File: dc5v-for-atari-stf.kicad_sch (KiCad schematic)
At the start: 13 parts, among them J1 Conn_01x02, J2 Conn_01x06, J3 Adjustable MT3608 module, J4 Fixed 12V module, J5 Conn_01x02, SW1 Momentary or Latched

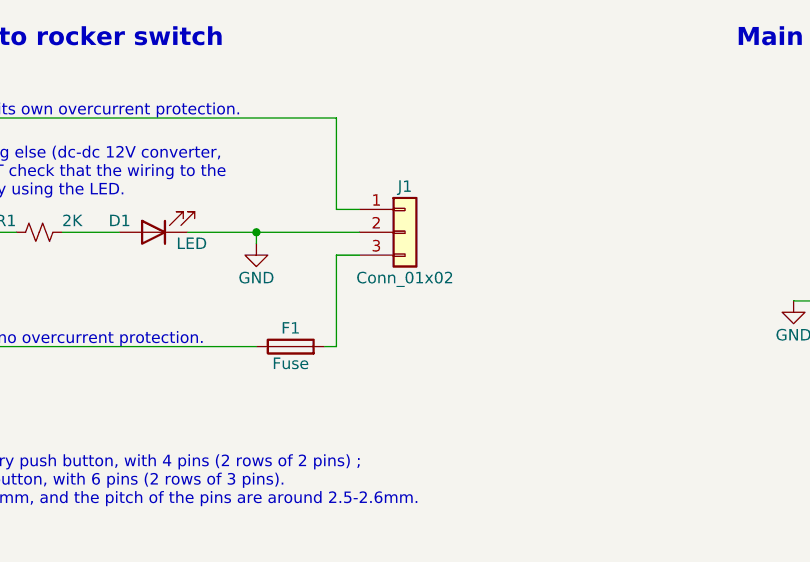
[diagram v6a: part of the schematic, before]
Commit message: schematic : associate footprints to J1 and F1
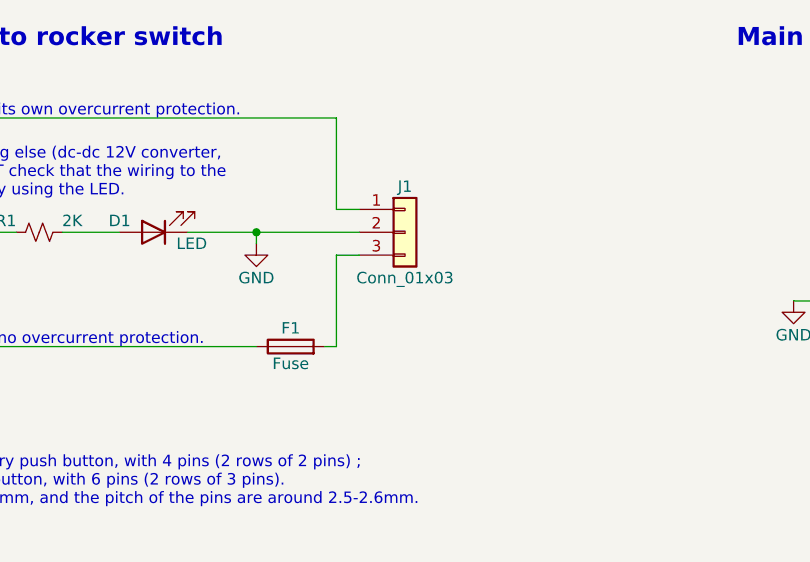
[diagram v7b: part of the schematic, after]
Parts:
- F1: footprint (none) -> commons-passives_THT:FuseHolder_Cylinder_5x20mm_Wurth_Elektronik_696310001002
- J1: value Conn_01x02 -> Conn_01x03; footprint commons-interconnect_THT:Fixed_Terminal_Blocks_Wurth_Elektronik_Serie_4122_7.00mm_Screwless_45degrees_1x02 -> commons-interconnect_THT:Fixed_Terminal_Blocks_Wurth_Elektronik_Serie_4122_7.00mm_Screwless_45degrees_1x03
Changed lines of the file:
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@@
     (in_bom yes) (on_board yes)
     (property "Reference" "J1" (id 0) (at 93.98 40.64 0))
-    (property "Value" "Conn_01x02" (id 1) (at 93.98 50.8 0))
-    (property "Footprint" "commons-interconnect_THT:Fixed_Terminal_Blocks_Wurth_Elektronik_Serie_4122_7.00mm_Screwless_45degrees_1x02" (id 2) (at 93.98 45.72 0)
+    (property "Value" "Conn_01x03" (id 1) (at 93.98 50.8 0))
+    (property "Footprint" "commons-interconnect_THT:Fixed_Terminal_Blocks_Wurth_Elektronik_Serie_4122_7.00mm_Screwless_45degrees_1x03" (id 2) (at 93.98 45.72 0)
       (effects (font (size 1.27 1.27)) hide)
     )
@@
     (property "Reference" "F1" (id 0) (at 81.28 56.388 90))
     (property "Value" "Fuse" (id 1) (at 81.28 60.325 90))
-    (property "Footprint" "" (id 2) (at 81.28 60.198 90)
+    (property "Footprint" "commons-passives_THT:FuseHolder_Cylinder_5x20mm_Wurth_Elektronik_696310001002" (id 2) (at 81.28 60.198 90)
       (effects (font (size 1.27 1.27)) hide)
     )
@@
     )
     (path "/e154b2a8-7971-4d03-8a83-71e2cbb0cd17"
-      (reference "F1") (unit 1) (value "Fuse") (footprint "")
+      (reference "F1") (unit 1) (value "Fuse") (footprint "commons-passives_THT:FuseHolder_Cylinder_5x20mm_Wurth_Elektronik_696310001002")
     )
     (path "/42ff79f5-7aba-4233-be21-4072d4762c22"
@@
     )
     (path "/9d541d6f-313d-4469-a000-68242c1dd6d6"
-      (reference "J1") (unit 1) (value "Conn_01x02") (footprint "commons-interconnect_THT:Fixed_Terminal_Blocks_Wurth_Elektronik_Serie_4122_7.00mm_Screwless_45degrees_1x02")
+      (reference "J1") (unit 1) (value "Conn_01x03") (footprint "commons-interconnect_THT:Fixed_Terminal_Blocks_Wurth_Elektronik_Serie_4122_7.00mm_Screwless_45degrees_1x03")
     )
     (path "/668b82fe-b542-4bd0-b2a5-5dae0ac43510"

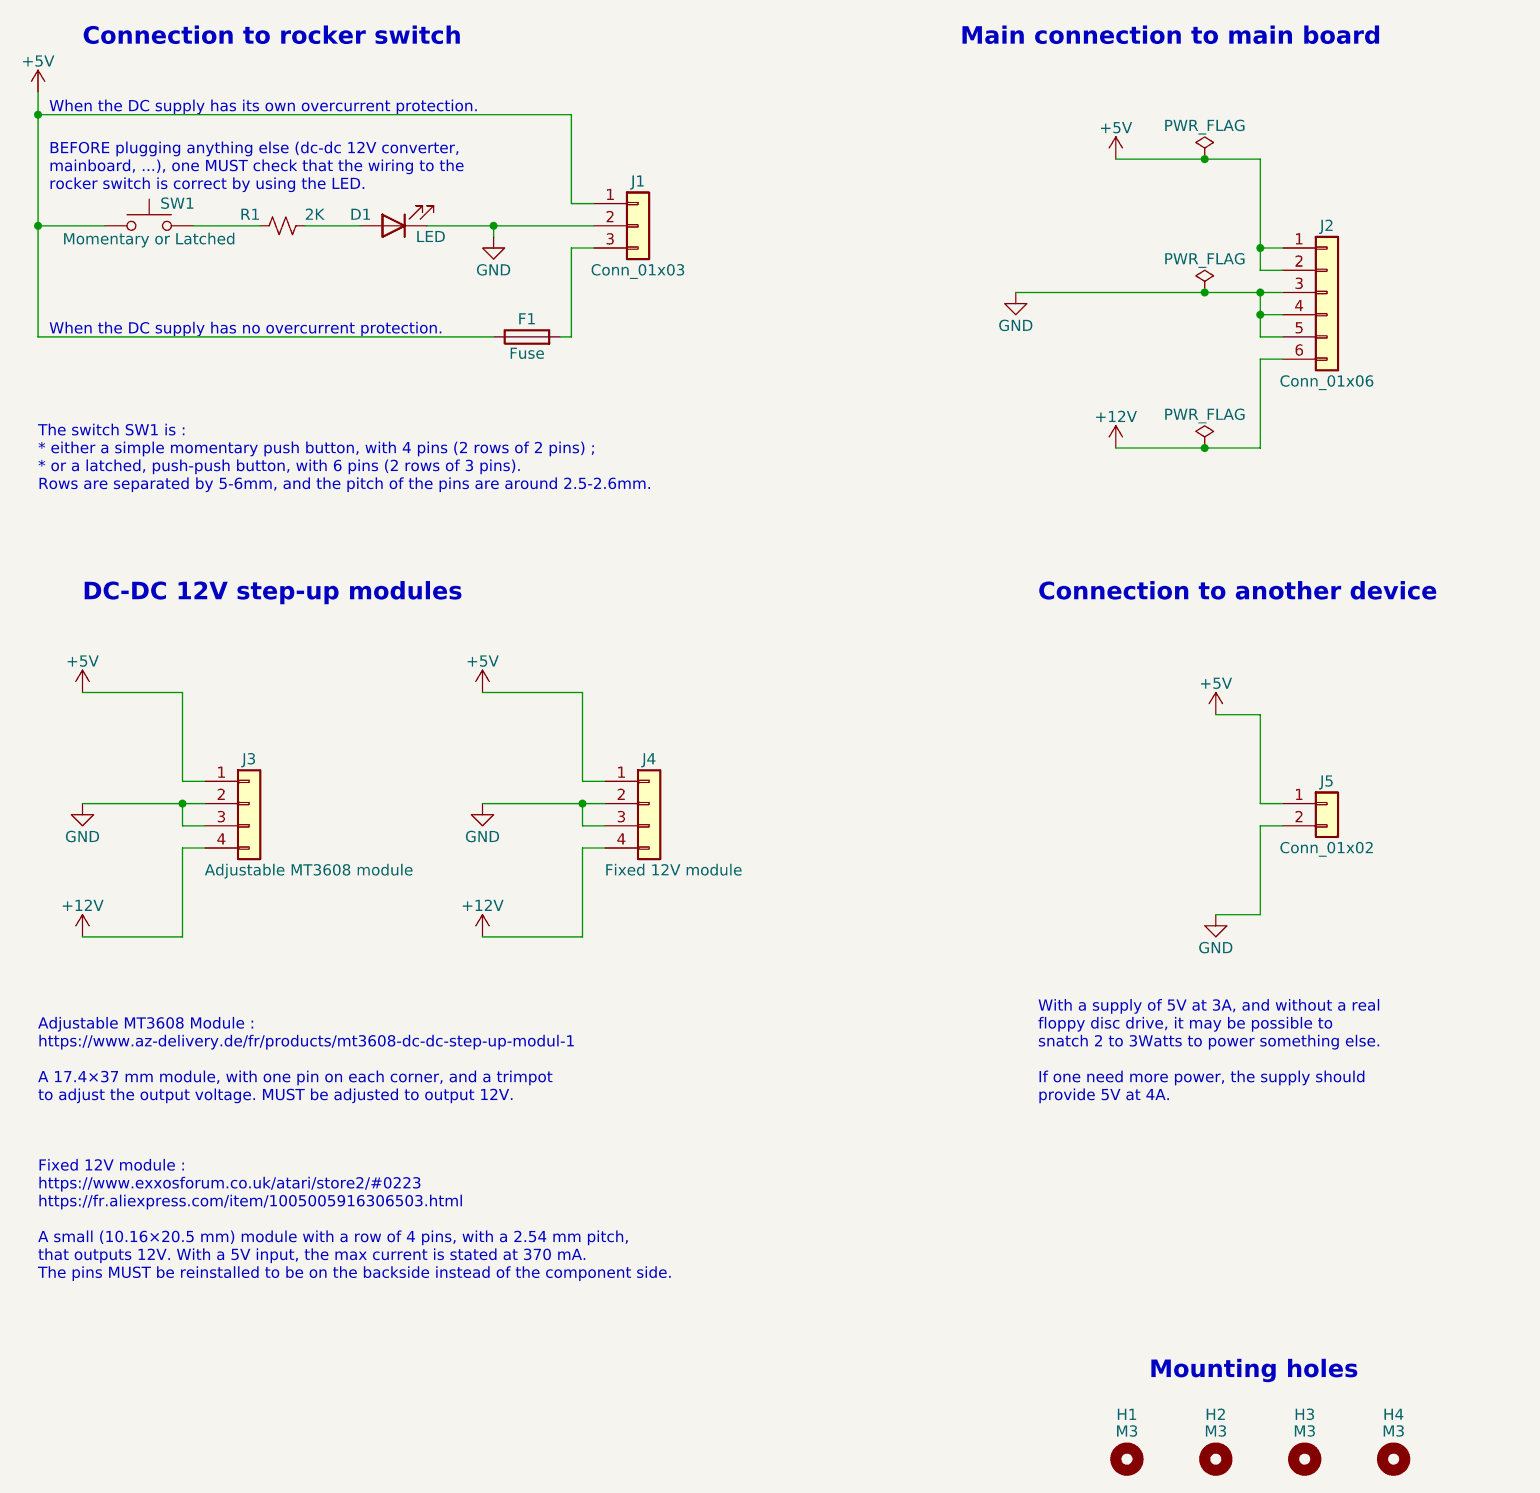
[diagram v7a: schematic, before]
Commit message: add references to part numbers
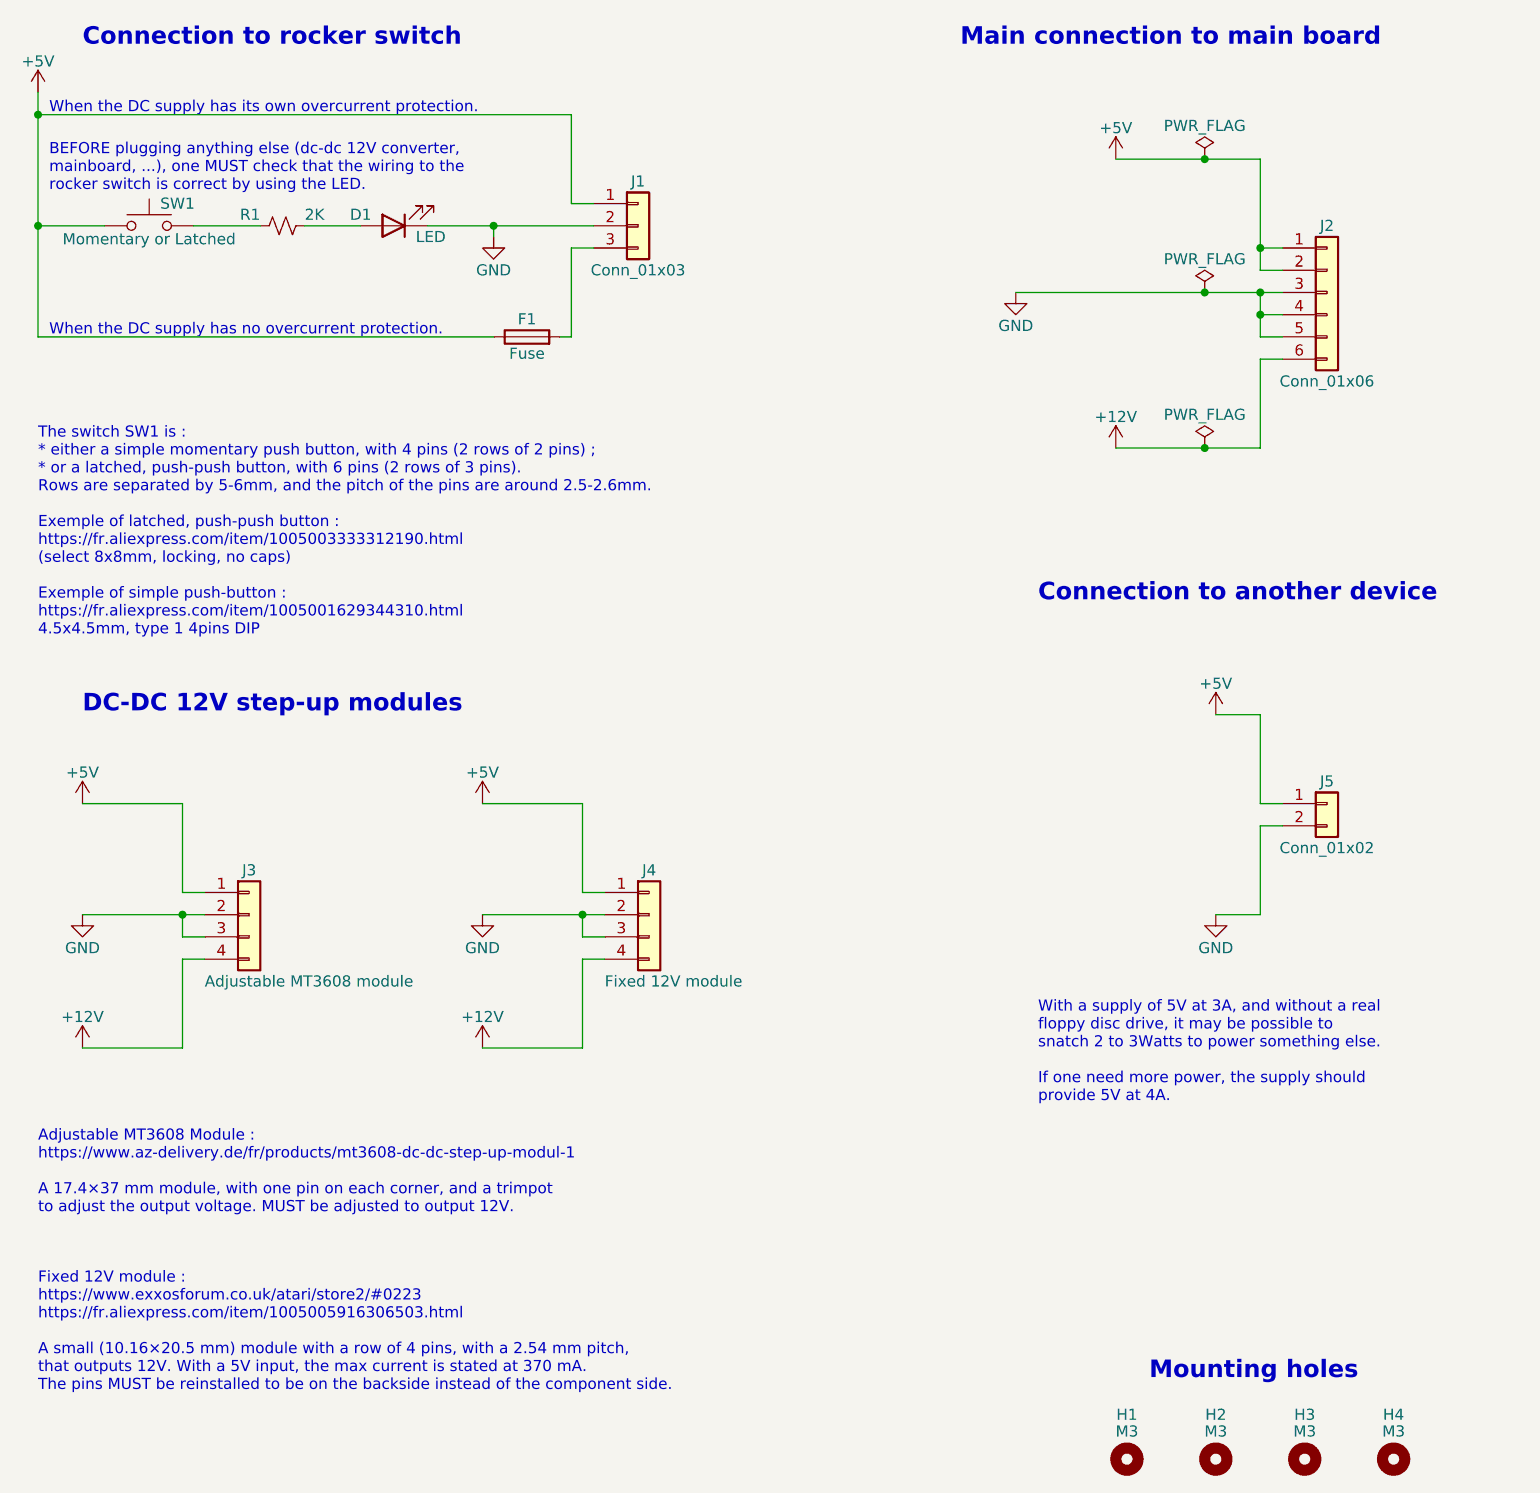
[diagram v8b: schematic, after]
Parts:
- F1: Mouser part number (none) -> 710-696310001002
- J1: Mouser part number (none) -> 710-691412220003
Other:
- note added: "The switch SW1 is : * either a simple momentary push button, with 4 pins (2 rows of 2 pins) ; * or a latched, push-push button, with 6 pins (2 rows of 3 pins). Rows are separated by 5-6mm, and the pitch of the pins are around 2.5-2.6mm. Exemple of latched, push-push button : https://fr.aliexpress.com/item/1005003333312190.html (select 8x8mm, locking, no caps) Exemple of simple push-button : https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"
- note removed: "The switch SW1 is : * either a simple momentary push button, with 4 pins (2 rows of 2 pins) ; * or a latched, push-push button, with 6 pins (2 rows of 3 pins). Rows are separated by 5-6mm, and the pitch of the pins are around 2.5-2.6mm."
- moved on the sheet: J3, J4
